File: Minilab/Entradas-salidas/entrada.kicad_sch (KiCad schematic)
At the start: 69 parts, among them J1 Out 5V/0V, J10 Vin, J11 Vin, J12 Vin, J13 Vin, J15 Vin, J16 Vin, J17 VCC, J18 OUT, J19 GND, J2 Out 5V/0V, J20 Conn_01x08_Pin, J21 Conn_01x08_Pin, J3 Out 5V/0V, J4 Out 5V/0V, J5 Out 5V/0V, J6 Out 5V/0V, J7 Vin, J8 Vin, J9 Vin, SW1 SW_SPST, SW2 SW_SPST, SW3 SW_SPST, SW4 SW_SPST, SW5 SW_SPST, SW6 SW_SPST, U1 4049, U10 NE555P, U2 Mini360

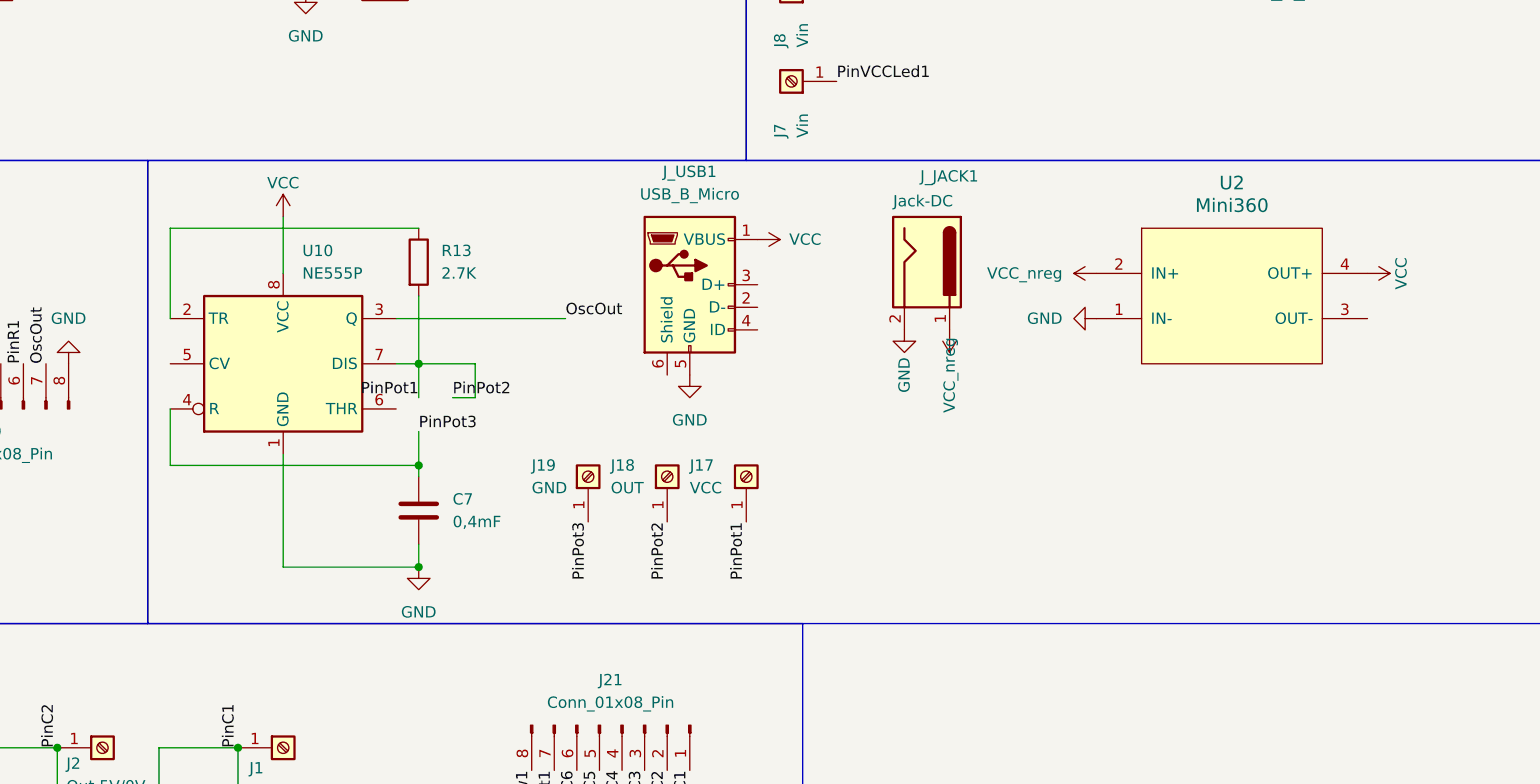
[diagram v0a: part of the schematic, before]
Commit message: cambio oscilador
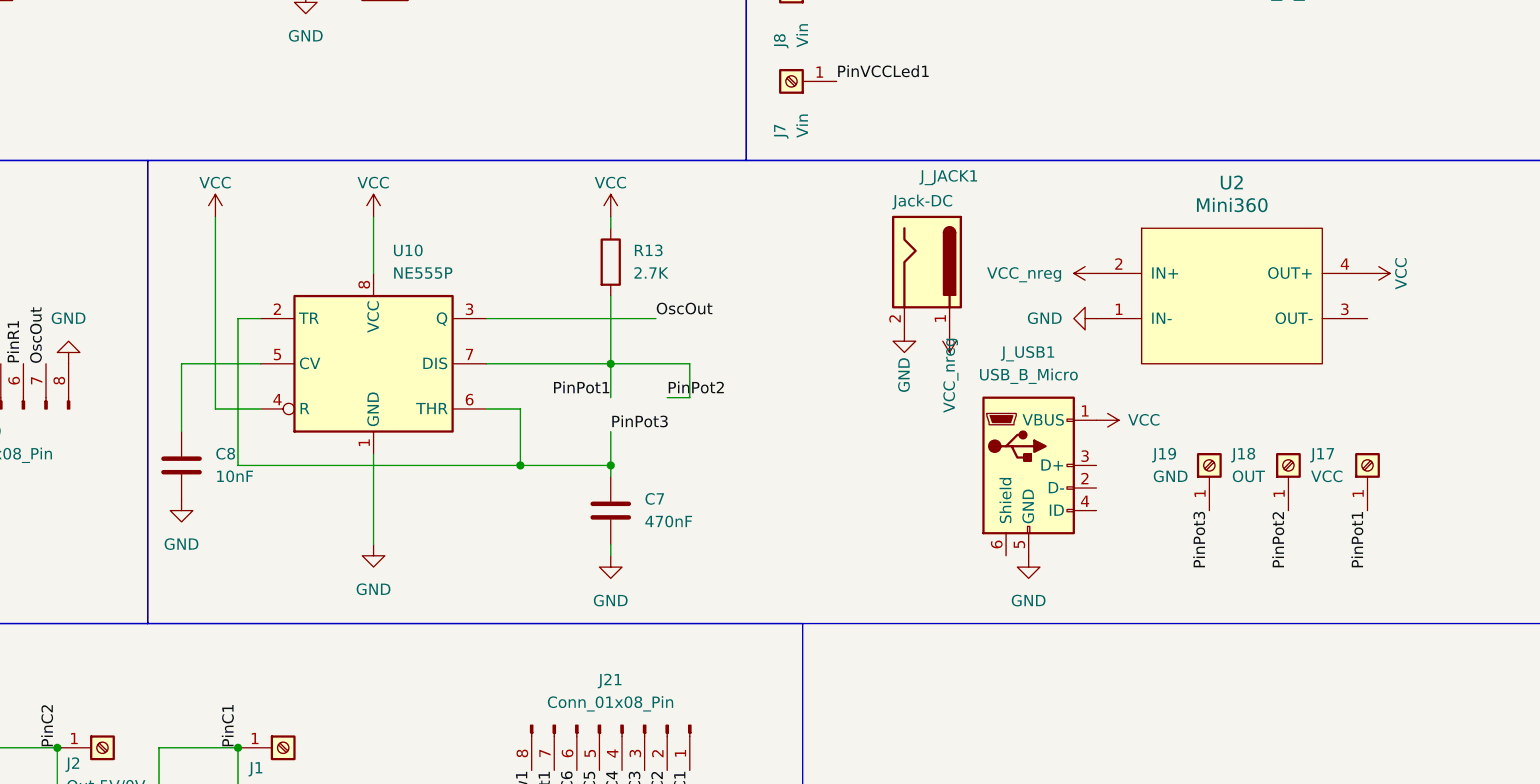
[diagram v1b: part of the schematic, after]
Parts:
- added C8: 10nF, Capacitor_THT:C_Disc_D5.0mm_W2.5mm_P2.50mm, symbol Device:C
- C7: value 0,4mF -> 470nF; footprint (none) -> Capacitor_THT:C_Disc_D5.0mm_W2.5mm_P2.50mm
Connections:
- net GND: now also C8.2
- net PinPot3: now also U10.2 (TR), U10.6 (THR); no longer U10.4 (R)
- net VCC: now also R13.1, U10.4 (R)
- net at U10.5 (CV): now also C8.1
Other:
- moved on the sheet: C7, J17, J18, J19, J_USB1, R13, U10

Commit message: update
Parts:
- J_USB1: footprint Connector_USB:USB_Micro-B_Molex_47346-0001 -> minilab:usb
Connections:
- net GND: now also J_USB1.4 (ID)
- net VCC: now also J_USB1.2 (D-)
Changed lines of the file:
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@@
 	)
 	(junction
+		(at 219.71 129.54)
+		(diameter 0)
+		(color 0 0 0 0)
+	)
+	(junction
 		(at 91.44 149.86)
 		(diameter 0)
@@
 	)
 	(junction
+		(at 228.6 113.03)
+		(diameter 0)
+		(color 0 0 0 0)
+	)
+	(junction
 		(at 113.03 64.77)
 		(diameter 0)
@@
 	(wire
 		(pts
+			(xy 227.33 120.65) (xy 228.6 120.65)
+		)
+		(stroke
+			(width 0)
+			(type default)
+		)
+	)
+	(wire
+		(pts
 			(xy 36.83 170.18) (xy 36.83 179.07)
 		)
@@
 	(wire
 		(pts
+			(xy 227.33 123.19) (xy 227.33 129.54)
+		)
+		(stroke
+			(width 0)
+			(type default)
+		)
+	)
+	(wire
+		(pts
 			(xy 156.21 38.1) (xy 156.21 39.37)
 		)
@@
 	(wire
 		(pts
+			(xy 219.71 129.54) (xy 219.71 128.27)
+		)
+		(stroke
+			(width 0)
+			(type default)
+		)
+	)
+	(wire
+		(pts
 			(xy 106.68 64.77) (xy 113.03 64.77)
 		)
@@
 	(wire
 		(pts
+			(xy 228.6 113.03) (xy 227.33 113.03)
+		)
+		(stroke
+			(width 0)
+			(type default)
+		)
+	)
+	(wire
+		(pts
 			(xy 128.27 111.76) (xy 133.35 111.76)
 		)
@@
 	(wire
 		(pts
+			(xy 219.71 129.54) (xy 227.33 129.54)
+		)
+		(stroke
+			(width 0)
+			(type default)
+		)
+	)
+	(wire
+		(pts
 			(xy 121.92 149.86) (xy 130.81 149.86)
 		)
@@
 	(wire
 		(pts
+			(xy 219.71 130.81) (xy 219.71 129.54)
+		)
+		(stroke
+			(width 0)
+			(type default)
+		)
+	)
+	(wire
+		(pts
 			(xy 172.72 106.68) (xy 181.61 106.68)
 		)
@@
 	(wire
 		(pts
+			(xy 228.6 113.03) (xy 228.6 120.65)
+		)
+		(stroke
+			(width 0)
+			(type default)
+		)
+	)
+	(wire
+		(pts
 			(xy 110.49 179.07) (xy 110.49 184.15)
 		)
@@
 			)
 		)
-		(property "Footprint" "Connector_USB:USB_Micro-B_Molex_47346-0001"
+		(property "Footprint" "minilab:usb"
 			(at 223.52 119.38 0)
 			(effects
@@
 	(symbol
 		(lib_id "power:VCC")
-		(at 227.33 113.03 270)
+		(at 228.6 113.03 270)
 		(unit 1)
 		(exclude_from_sim no)
@@
 		(dnp no)
 		(property "Reference" "#PWR01"
-			(at 223.52 113.03 0)
+			(at 224.79 113.03 0)
 			(effects
 				(font
@@
 		)
 		(property "Value" "VCC"
-			(at 230.886 113.03 90)
+			(at 232.156 113.03 90)
 			(effects
 				(font
@@
 		)
 		(property "Footprint" ""
-			(at 227.33 113.03 0)
+			(at 228.6 113.03 0)
 			(effects
 				(font
@@
 		)
 		(property "Datasheet" ""
-			(at 227.33 113.03 0)
+			(at 228.6 113.03 0)
 			(effects
 				(font
@@
 		)
 		(property "Description" "Power symbol creates a global label with name \"VCC\""
-			(at 227.33 113.03 0)
+			(at 228.6 113.03 0)
 			(effects
 				(font
@@
 		(lib_name "GND_1")
 		(lib_id "power:GND")
-		(at 219.71 128.27 0)
+		(at 219.71 130.81 0)
 		(unit 1)
 		(exclude_from_sim no)
@@
 		(fields_autoplaced yes)
 		(property "Reference" "#PWR03"
-			(at 219.71 134.62 0)
+			(at 219.71 137.16 0)
 			(effects
 				(font
@@
 		)
 		(property "Value" "GND"
-			(at 219.71 133.35 0)
+			(at 219.71 135.89 0)
 			(effects
 				(font
@@
 		)
 		(property "Footprint" ""
-			(at 219.71 128.27 0)
+			(at 219.71 130.81 0)
 			(effects
 				(font
@@
 		)
 		(property "Datasheet" ""
-			(at 219.71 128.27 0)
+			(at 219.71 130.81 0)
 			(effects
 				(font
@@
 		)
 		(property "Description" "Power symbol creates a global label with name \"GND\" , ground"
-			(at 219.71 128.27 0)
+			(at 219.71 130.81 0)
 			(effects
 				(font
